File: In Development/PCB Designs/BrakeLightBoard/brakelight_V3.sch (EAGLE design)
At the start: 21 parts, among them Q2 30N06L

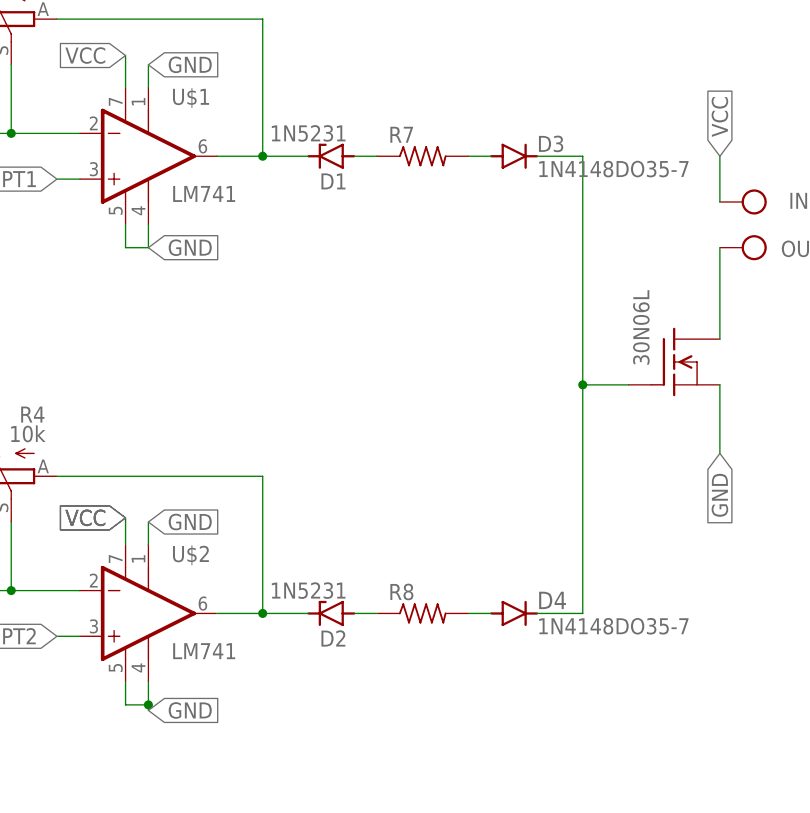
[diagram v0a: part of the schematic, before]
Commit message: Added missing resistor values
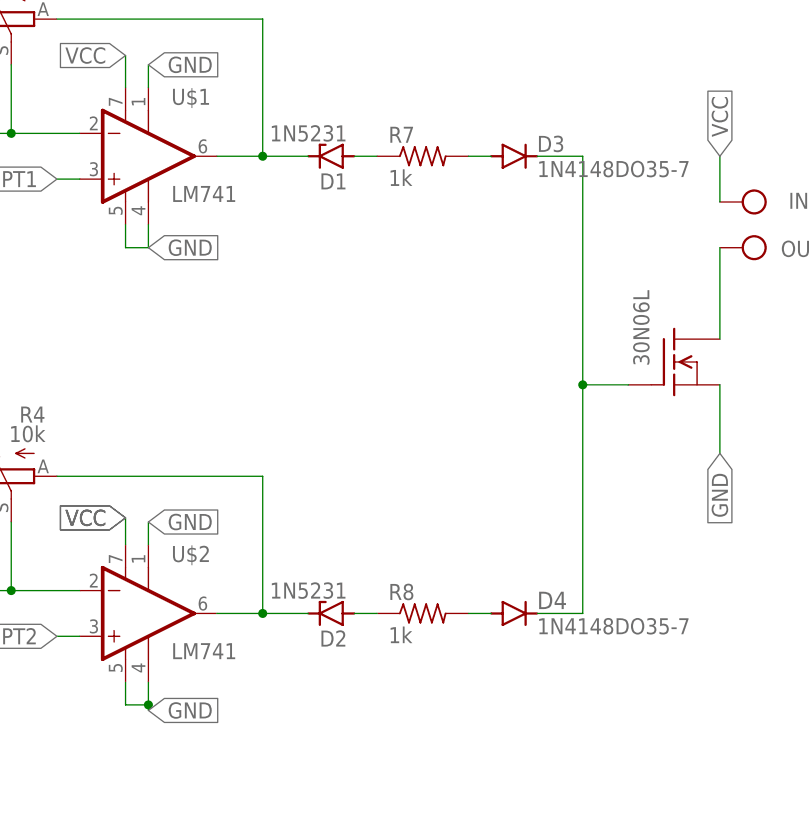
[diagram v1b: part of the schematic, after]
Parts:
- R7, R8: value (none) -> 1k
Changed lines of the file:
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@@
 <part name="D3" library="diode" library_urn="urn:adsk.eagle:library:210" deviceset="1N4148" device="DO35-7" package3d_urn="urn:adsk.eagle:package:43339/2"/>
 <part name="D4" library="diode" library_urn="urn:adsk.eagle:library:210" deviceset="1N4148" device="DO35-7" package3d_urn="urn:adsk.eagle:package:43339/2"/>
-<part name="R7" library="0ohmresistor" deviceset="R-US_" device="0204/5" package3d_urn="urn:adsk.eagle:package:23488/1"/>
-<part name="R8" library="0ohmresistor" deviceset="R-US_" device="0204/5" package3d_urn="urn:adsk.eagle:package:23488/1"/>
+<part name="R7" library="0ohmresistor" deviceset="R-US_" device="0204/5" package3d_urn="urn:adsk.eagle:package:23488/1" value="1k"/>
+<part name="R8" library="0ohmresistor" deviceset="R-US_" device="0204/5" package3d_urn="urn:adsk.eagle:package:23488/1" value="1k"/>
 </parts>
 <sheets>

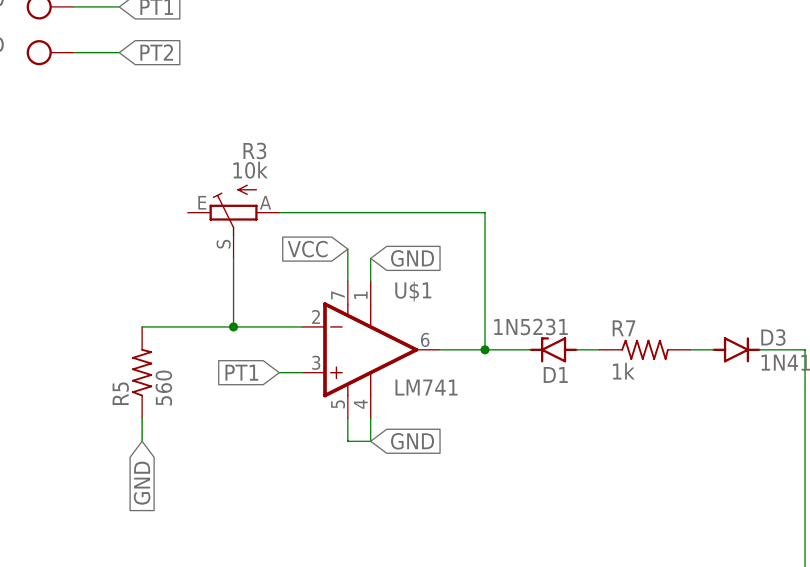
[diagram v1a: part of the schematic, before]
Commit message: Created new brakelight board using TLC2252
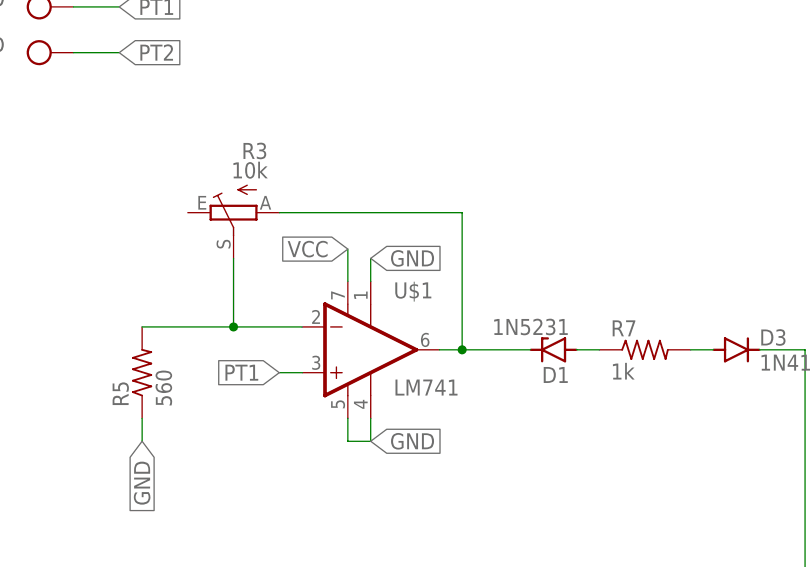
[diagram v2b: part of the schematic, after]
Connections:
- new net N$8: D1.C, R3.A, U$1.OUT
- net 5V: no longer D1.C, R3.A, U$1.OUT
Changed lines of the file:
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@@
 <label x="-40.64" y="-30.48" size="1.778" layer="95" xref="yes"/>
-</segment>
-<segment>
-<pinref part="U$1" gate="G$1" pin="OUT"/>
-<wire x1="43.18" y1="10.16" x2="48.26" y2="10.16" width="0.1524" layer="91"/>
-<pinref part="R3" gate="1" pin="A"/>
-<wire x1="48.26" y1="10.16" x2="48.26" y2="25.4" width="0.1524" layer="91"/>
-<wire x1="48.26" y1="25.4" x2="25.4" y2="25.4" width="0.1524" layer="91"/>
-<junction x="48.26" y="10.16"/>
-<wire x1="48.26" y1="10.16" x2="53.34" y2="10.16" width="0.1524" layer="91"/>
-<pinref part="D1" gate="G$1" pin="C"/>
 </segment>
 </net>
@@
 </segment>
 </net>
+<net name="N$8" class="0">
+<segment>
+<pinref part="R3" gate="1" pin="A"/>
+<wire x1="25.4" y1="25.4" x2="45.72" y2="25.4" width="0.1524" layer="91"/>
+<pinref part="U$1" gate="G$1" pin="OUT"/>
+<wire x1="45.72" y1="25.4" x2="45.72" y2="10.16" width="0.1524" layer="91"/>
+<wire x1="45.72" y1="10.16" x2="43.18" y2="10.16" width="0.1524" layer="91"/>
+<pinref part="D1" gate="G$1" pin="C"/>
+<wire x1="53.34" y1="10.16" x2="45.72" y2="10.16" width="0.1524" layer="91"/>
+<junction x="45.72" y="10.16"/>
+</segment>
+</net>
